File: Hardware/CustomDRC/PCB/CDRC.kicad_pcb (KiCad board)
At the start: 2 copper layers, 76.5 x 28.2 mm, 54 parts, among them IC301 SN65HVD75DR, J101 DSP Header, J401 TC2030NL - For UART PROG, J501 Conn_01x05, J504 Conn_01x05, Q501 AO3401A, Q502 AO3400A, U401 ESP32-WROOM-32UE-R2, U501 ESD224DQA, U502 ESD224DQA

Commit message: Update - finished schematic for revision A
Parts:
- removed JP301: SolderJumper_2_Open, Jumper:SolderJumper-2_P1.3mm_Open_RoundedPad1.0x1.5mm
- removed Q502: AO3400A, Package_TO_SOT_SMD:SOT-23
- added C201: 0u1, Capacitor_SMD:C_0603_1608Metric_Pad1.08x0.95mm_HandSolder, F.Cu at (153.0, 78.0)
- added C202: 10u, Capacitor_SMD:C_1206_3216Metric_Pad1.33x1.80mm_HandSolder, F.Cu at (154.0, 69.5)
- added C203: 10u, Capacitor_SMD:C_1206_3216Metric_Pad1.33x1.80mm_HandSolder, F.Cu at (154.0, 72.0)
- added C204: 22u, Capacitor_SMD:C_0805_2012Metric_Pad1.18x1.45mm_HandSolder, F.Cu at (147.5, 70.2)
- added C205: 22u, Capacitor_SMD:C_0805_2012Metric_Pad1.18x1.45mm_HandSolder, F.Cu at (147.5, 72.2)
- added C206: 2u2, Capacitor_SMD:C_0805_2012Metric_Pad1.18x1.45mm_HandSolder, F.Cu at (143.5, 75.0)
- added C207: 2u2, Capacitor_SMD:C_0805_2012Metric_Pad1.18x1.45mm_HandSolder, F.Cu at (137.5, 75.0)
- added C401: 1u, Capacitor_SMD:C_0603_1608Metric_Pad1.08x0.95mm_HandSolder, F.Cu at (118.0, 55.2)
- added C402: 22u, Capacitor_SMD:C_0805_2012Metric_Pad1.18x1.45mm_HandSolder, F.Cu at (113.5, 57.5)
- added C403: 1u, Capacitor_SMD:C_0603_1608Metric_Pad1.08x0.95mm_HandSolder, F.Cu at (115.5, 57.8)
- added D201: 1N4148WS, Diode_SMD:D_SOD-323_HandSoldering, F.Cu at (140.5, 72.0)
- added D202: US1M, Diode_SMD:D_SMA_Handsoldering, F.Cu at (158.2, 74.0)
- added D401: LED_Small, LED_SMD:LED_0603_1608Metric_Pad1.05x0.95mm_HandSolder, F.Cu at (126.0, 77.7)
- added F201: 2A TRIP, Fuse:Fuse_1206_3216Metric_Pad1.42x1.75mm_HandSolder, F.Cu at (161.5, 74.0)
- added F202: 1A TRIP, Fuse:Fuse_0603_1608Metric_Pad1.05x0.95mm_HandSolder, F.Cu at (137.5, 71.0)
- added H101: MountingHole, MountingHole:MountingHole_2.7mm_M2.5, F.Cu at (156.8, 55.2)
- added H102: MountingHole, MountingHole:MountingHole_2.7mm_M2.5, F.Cu at (97.8, 66.2)
- added H103: MountingHole, MountingHole:MountingHole_2.7mm_M2.5, F.Cu at (167.2, 76.8)
- added J502: JST-PH-2.0-02, Connector_JST:JST_PH_B2B-PH-K_1x02_P2.00mm_Vertical, F.Cu at (103.8, 67.2)
- added JP304: SolderJumper_3_Bridged12, Jumper:SolderJumper-3_P1.3mm_Bridged2Bar12_RoundedPad1.0x1.5mm, F.Cu at (144.8, 64.2)
- added L201: 4u7, Inductor_SMD:L_Chilisin_BMRA00040420, F.Cu at (148.5, 76.0)
- added R201: 0R, Resistor_SMD:R_0603_1608Metric_Pad0.98x0.95mm_HandSolder, F.Cu at (142.7, 68.6)
- added R401: 10k, Resistor_SMD:R_0603_1608Metric_Pad0.98x0.95mm_HandSolder, F.Cu at (114.5, 60.2)
- added R402: 330R, Resistor_SMD:R_0603_1608Metric_Pad0.98x0.95mm_HandSolder, F.Cu at (115.2, 76.2)
- added R403: 330R, Resistor_SMD:R_0603_1608Metric_Pad0.98x0.95mm_HandSolder, F.Cu at (138.5, 68.2)
- added TP101: TestPoint_Small, TestPoint:TestPoint_Keystone_5000-5004_Miniature, F.Cu at (163.5, 59.0)
- added TP102: TestPoint_Small, TestPoint:TestPoint_Pad_D1.5mm, F.Cu at (164.0, 71.8)
- added TP103: TestPoint_Small, TestPoint:TestPoint_Pad_D1.5mm, F.Cu at (155.8, 66.8)
- added TP201: TestPoint_Small, TestPoint:TestPoint_Pad_D1.5mm, F.Cu at (150.2, 68.2)
- added TP202: TestPoint_Small, TestPoint:TestPoint_Pad_D1.5mm, F.Cu at (135.0, 77.8)
- added TP203: TestPoint_Small, TestPoint:TestPoint_Pad_D1.5mm, F.Cu at (144.2, 71.2)
- added TP204: TestPoint_Small, TestPoint:TestPoint_Pad_D1.5mm, F.Cu at (158.2, 67.8)
- added TP401: TestPoint_Small, TestPoint:TestPoint_Pad_D1.5mm, F.Cu at (130.5, 78.0)
- added U201: AP63205WU-7, Package_TO_SOT_SMD:TSOT-23-6, F.Cu at (153.8, 75.0)
- added U202: TLV76733DRVR, Package_SON:WSON-6-1EP_2x2mm_P0.65mm_EP1x1.6mm_ThermalVias, F.Cu at (140.5, 74.5)
- C301: footprint Capacitor_SMD:C_0603_1608Metric -> Capacitor_SMD:C_0603_1608Metric_Pad1.08x0.95mm_HandSolder
- D301: value SM712_SOT23 -> SM712
- IC301: footprint Package_SO:SOIC-8_5.23x5.23mm_P1.27mm -> Package_SO:SOIC-8_3.9x4.9mm_P1.27mm
- J501, J504: value Conn_01x05 -> JST-PH-2.0-05
- Q501: value AO3401A -> AO3400A
- R501, R503: value 10k -> 330R
- R502, R504, R510, R511, R512, R515: value 330R -> 10k
- TP508: footprint TestPoint:TestPoint_Pad_D1.5mm -> TestPoint:TestPoint_Keystone_5000-5004_Miniature
- moved Q501 44.8 mm to (99.2, 71.0), turned to 90 degrees
- moved R505 40.1 mm to (96.5, 70.8), turned to -90 degrees
- moved R501 38.8 mm to (97.8, 61.2), turned to 0 degrees
- moved TP306 36.8 mm to (117.5, 77.8), turned to 0 degrees
- moved TP304 36.0 mm to (120.5, 77.8)
- moved R503 32.7 mm to (113.8, 76.2)
- moved TP301 27.1 mm to (140.2, 66.2)
- moved TP302 22.6 mm to (138.0, 65.0)
- moved TP307 18.6 mm to (158.0, 59.5)
- moved TP305 18.4 mm to (150.2, 56.8)
- moved TP303 16.5 mm to (140.2, 62.8)
- moved C301 8.73 mm to (154.8, 59.2), turned to 0 degrees
- moved R301 8.65 mm to (148.5, 58.8)
- moved IC301 8.57 mm to (151.5, 62.8)
- moved R302 8.57 mm to (158.0, 61.8)
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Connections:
- C301 pad 1: Net-(IC301-VCC) -> VCC
- C501 pad 1: /USER_INTERFACE/ENCODER_1_B -> /MCU/IO32
- C502 pad 1: /USER_INTERFACE/ENCODER_1_A -> /MCU/IO35
- C503 pad 1: /USER_INTERFACE/ENCODER_2_B -> /MCU/GPIO39
- C504 pad 1: /USER_INTERFACE/ENCODER_2_A -> /MCU/GPIO36
- C505 pad 1: /USER_INTERFACE/ENCODER_1_SW -> /MCU/IO33
- C506 pad 1: /USER_INTERFACE/ENCODER_2_SW -> /MCU/IO34
- IC301 pad 1: /RS485/RX485_RX -> /MCU/IO21
- IC301 pad 2: /RS485/RS485_TX_EN -> /RS485/~{RE}
- IC301 pad 3: /RS485/RS485_TX_EN -> /MCU/IO19
- IC301 pad 4: /RS485/RX485_TX -> /MCU/IO18
- IC301 pad 8: Net-(IC301-VCC) -> VCC
- J101 pad 1: GND -> unconnected-(J101-Pin_1-Pad1)
- J101 pad 3: /DSP_RS485_B/Z -> GND
- J101 pad 4: /DSP_RS485_A/Y -> /DSP_RS485_B/Z
- J101 pad 5: /DSP_POWER_EN -> /DSP_RS485_A/Y
- J101 pad 6: /DSP_CONST_12V -> /DSP_POWER_EN
- J101 pad 7: unconnected-(J101-Pin_7-Pad7) -> /DSP_CONST_12V
- J501 pad 1: /USER_INTERFACE/ENC_3_A -> /USER_INTERFACE/ENC_2_A
- Q501 pad 2: VCC -> GND
- Q501 pad 3: VCC_ENCODER -> Net-(J502-Pin_1)
- R301 pad 1: Net-(IC301-VCC) -> VCC
- R301 pad 2: /RS485/RX485_RX -> /MCU/IO21
- R305 pad 1: /RS485/RS485_TX_EN -> /MCU/IO19
- R501 pad 1: VCC -> +5V
- R501 pad 2: Net-(Q501-G) -> Net-(J502-Pin_2)
- R502 pad 1: /USER_INTERFACE/ENC_1_B -> /MCU/IO32
- R502 pad 2: /USER_INTERFACE/ENCODER_1_B -> /USER_INTERFACE/ENC_1_B
- R503 pad 1: /USER_INTERFACE/ENCODER_PWR_EN -> /MCU/IO25
- R503 pad 2: GND -> Net-(Q501-G)
- R504 pad 2: /USER_INTERFACE/ENCODER_1_A -> /MCU/IO35
- R505 pad 1: Net-(Q502-G) -> GND
- R505 pad 2: /USER_INTERFACE/ENCODER_PWR_EN -> Net-(Q501-G)
- R506 pad 1: /USER_INTERFACE/ENCODER_1_A -> /USER_INTERFACE/ENC_1_A
- R506 pad 2: VCC_ENCODER -> VCC
- R507 pad 1: /USER_INTERFACE/ENCODER_1_B -> /USER_INTERFACE/ENC_1_B
- R507 pad 2: VCC_ENCODER -> VCC
- R508 pad 1: /USER_INTERFACE/ENCODER_2_B -> /USER_INTERFACE/ENC_2_B
- R508 pad 2: VCC_ENCODER -> VCC
- R509 pad 1: /USER_INTERFACE/ENCODER_2_A -> /USER_INTERFACE/ENC_2_A
- R509 pad 2: VCC_ENCODER -> VCC
- R510 pad 1: /USER_INTERFACE/ENC_2_B -> /MCU/GPIO39
- R510 pad 2: /USER_INTERFACE/ENCODER_2_B -> /USER_INTERFACE/ENC_2_B
- R511 pad 1: /USER_INTERFACE/ENC_3_A -> /USER_INTERFACE/ENC_2_A
- R511 pad 2: /USER_INTERFACE/ENCODER_2_A -> /MCU/GPIO36
- R512 pad 1: /USER_INTERFACE/ENC_1_SW -> /MCU/IO33
- R512 pad 2: /USER_INTERFACE/ENCODER_1_SW -> /USER_INTERFACE/ENC_1_SW
- R513 pad 1: /USER_INTERFACE/ENCODER_1_SW -> /USER_INTERFACE/ENC_1_SW
- R514 pad 1: /USER_INTERFACE/ENCODER_2_SW -> /USER_INTERFACE/ENC_2_SW
- R515 pad 1: /USER_INTERFACE/ENC_2_SW -> /MCU/IO34
- R515 pad 2: /USER_INTERFACE/ENCODER_2_SW -> /USER_INTERFACE/ENC_2_SW
- TP301 pad 1: /RS485/RX485_TX -> /MCU/IO18
- TP302 pad 1: /RS485/RS485_TX_EN -> /MCU/IO19
- TP303 pad 1: /RS485/RX485_RX -> /MCU/IO21
- TP304 pad 1: /DSP_RS485_B/Z -> Net-(U401-IO26)
- TP305 pad 1: Net-(IC301-VCC) -> VCC
- TP306 pad 1: /DSP_RS485_A/Y -> Net-(U401-IO27)
- TP501 pad 1: /USER_INTERFACE/ENCODER_1_B -> /MCU/IO32
- TP502 pad 1: /USER_INTERFACE/ENCODER_1_A -> /MCU/IO35
- TP503 pad 1: /USER_INTERFACE/ENCODER_1_SW -> /MCU/IO33
- TP504 pad 1: /USER_INTERFACE/ENCODER_2_B -> /MCU/GPIO39
- TP505 pad 1: /USER_INTERFACE/ENCODER_2_A -> /MCU/GPIO36
- TP506 pad 1: /USER_INTERFACE/ENCODER_2_SW -> /MCU/IO34
- U401 pad 10: unconnected-(U401-IO25-Pad10) -> /MCU/IO25
- U401 pad 11: unconnected-(U401-IO26-Pad11) -> Net-(U401-IO26)
- U401 pad 12: unconnected-(U401-IO27-Pad12) -> Net-(U401-IO27)
- U401 pad 16: unconnected-(U401-IO13-Pad16) -> Net-(U401-IO13)
- U401 pad 29: unconnected-(U401-IO5-Pad29) -> /MCU/DSP_EN
- U401 pad 30: unconnected-(U401-IO18-Pad30) -> /MCU/IO18
- U401 pad 31: unconnected-(U401-IO19-Pad31) -> /MCU/IO19
- U401 pad 33: unconnected-(U401-IO21-Pad33) -> /MCU/IO21
- U401 pad 4: unconnected-(U401-SENSOR_VP-Pad4) -> /MCU/GPIO36
- U401 pad 5: unconnected-(U401-SENSOR_VN-Pad5) -> /MCU/GPIO39
- U401 pad 6: unconnected-(U401-IO34-Pad6) -> /MCU/IO34
- U401 pad 7: unconnected-(U401-IO35-Pad7) -> /MCU/IO35
- U401 pad 8: unconnected-(U401-IO32-Pad8) -> /MCU/IO32
- U401 pad 9: unconnected-(U401-IO33-Pad9) -> /MCU/IO33
- U502 pad 1: /USER_INTERFACE/ENC_3_A -> /USER_INTERFACE/ENC_2_A
- U502 pad 10: /USER_INTERFACE/ENC_3_A -> /USER_INTERFACE/ENC_2_A
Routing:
- net VCC: track 0.00 -> 136.6 mm
- net +5V: track 0.00 -> 100.8 mm
- net GND: track 0.00 -> 49.1 mm, vias 0 -> 45
- net /MCU/ESP_EN: track 0.00 -> 44.3 mm
- net /MCU/ESP_BOOT0: track 0.00 -> 29.4 mm
- net /DSP_POWER_EN: track 0.00 -> 29.2 mm
- net Net-(Q501-G): track 0.00 -> 28.6 mm
- net /USER_INTERFACE/ENC_2_B: track 0.00 -> 21.1 mm
- net /USER_INTERFACE/ENC_2_SW: track 0.00 -> 20.5 mm
- net /USER_INTERFACE/ENC_1_A: track 0.00 -> 19.6 mm
- net /MCU/IO19: track 0.00 -> 19.2 mm
- net /MCU/IO21: track 0.00 -> 18.8 mm
- net /USER_INTERFACE/ENC_1_SW: track 0.00 -> 18.3 mm
- net /USER_INTERFACE/ENC_2_A: track 0.00 -> 17.3 mm
- net /MCU/IO18: track 0.00 -> 16.5 mm
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- added copper zone on F.Cu, net +5V
- added copper zone on F.Cu, net /DSP_CONST_12V
- added copper zone on B.Cu, net GND
- added copper zone on F.Cu, net GND
- added copper zone on F.Cu, net Net-(D201-A)
- added copper zone on F.Cu, net Net-(D202-A)
- added copper zone on F.Cu, net Net-(D202-K)
- added copper zone on F.Cu, net Net-(F202-Pad2)
- added copper zone on F.Cu, net Net-(U201-SW)
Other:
- board size 76.5 x 28.2 mm -> 85 x 28.5 mm
- board text added: "${TITLE}-${REVISION} ${ISSUE_DATE}"
- board text added: "+"
- board text added: "-"
- board text added: "12V BLUE"
- board text added: "1A"
- board text added: "1B"
- board text added: "1SW"
- board text added: "2A"
- board text added: "2B"
- board text added: "2SW"
- board text added: "A/Y GREEN"
- board text added: "B/Z RED"
- board text added: "BLACK"
- board text added: "BLUE"
- board text added: "DNC"
- board text added: "ENC1"
- board text added: "ENC2"
- board text added: "GND"
- board text added: "GND BLACK"
- board text added: "GND WHITE"
- board text added: "GND YELLOW"
- board text added: "GREEN"
- board text added: "JAIME SEQUEIRA"
- board text added: "JLCJLCJLCJLC"
- board text added: "LED"
- board text added: "LED+"
- board text added: "LED-"
- board text added: "PROG"
- board text added: "RED"
- board text added: "WHITE"
- board text added: "YELLOW"

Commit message: Sync HW changes for V1 PCB
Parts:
- removed C206, C207: 2u2, Capacitor_SMD:C_0805_2012Metric_Pad1.18x1.45mm_HandSolder
- removed D201: 1N4148WS, Diode_SMD:D_SOD-323_HandSoldering
- removed F202: 1A TRIP, Fuse:Fuse_0603_1608Metric_Pad1.05x0.95mm_HandSolder
- removed TP202, TP305, TP307: TestPoint_Small, TestPoint:TestPoint_Pad_D1.5mm
- removed U202: TLV76733DRVR, Package_SON:WSON-6-1EP_2x2mm_P0.65mm_EP1x1.6mm_ThermalVias
- added R516: 330R, Resistor_SMD:R_1206_3216Metric_Pad1.30x1.75mm_HandSolder, F.Cu at (127.2, 87.5)
- D401: value LED_Small -> WHITE OR BLUE
- F201: value 2A TRIP -> BSMD1206-025-33V
- L201: footprint Inductor_SMD:L_Chilisin_BMRA00040420 -> Inductor_SMD:L_Cenker_CKCS4030
- U201: value AP63205WU-7 -> AP63203WU-7
- moved R201 40.9 mm to (173.8, 95.2)
- moved R403 40.0 mm to (168.0, 95.2)
- moved C503 39.5 mm to (141.5, 88.5)
- moved C501 39.5 mm to (141.5, 99.1)
- moved C502 39.5 mm to (141.5, 95.6)
- moved C505 39.5 mm to (141.5, 102.7)
- moved C506 39.5 mm to (141.5, 92.0)
- moved J101 39.5 mm to (196.8, 82.8)
- moved C201 39.5 mm to (182.5, 104.2)
- moved C202 39.5 mm to (183.5, 95.8)
- moved C203 39.5 mm to (183.5, 98.2)
- moved C204 39.5 mm to (177.0, 96.5)
- moved C205 39.5 mm to (177.0, 98.5)
- moved C301 39.5 mm to (184.2, 85.5)
- moved C401 39.5 mm to (147.5, 81.5)
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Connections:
- C204 pad 1: +5V -> VCC
- C205 pad 1: +5V -> VCC
- L201 pad 2: +5V -> VCC
- R201 pad 1: Net-(F202-Pad2) -> VCC
- R501 pad 1: +5V -> VCC
- TP203 pad 1: +5V -> VCC
- U201 pad 1: +5V -> VCC
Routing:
- net +5V: track 100.8 -> 0.00 mm
- net VCC: track 136.6 -> 168.5 mm
- net /MCU/IO19: track 19.2 -> 16.8 mm
- net /RS485/RS485_B: track 5.29 -> 3.26 mm
- net /RS485/RS485_A: track 4.79 -> 3.26 mm
- net /DSP_RS485_A/Y: track 14.6 -> 13.1 mm
- net GND: track 49.1 -> 47.7 mm, vias 45 -> 34
- net /MCU/ESP_EN: track 44.3 -> 43.1 mm
- net Net-(U201-SW): track 3.70 -> 2.56 mm
- net /MCU/IO34: track 9.21 -> 8.63 mm
- added copper zone on F.Cu, net VCC
- removed copper zone on F.Cu, net +5V
- removed copper zone on F.Cu, net Net-(D201-A)
- removed copper zone on F.Cu, net Net-(F202-Pad2)
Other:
- board text added: "MNT"

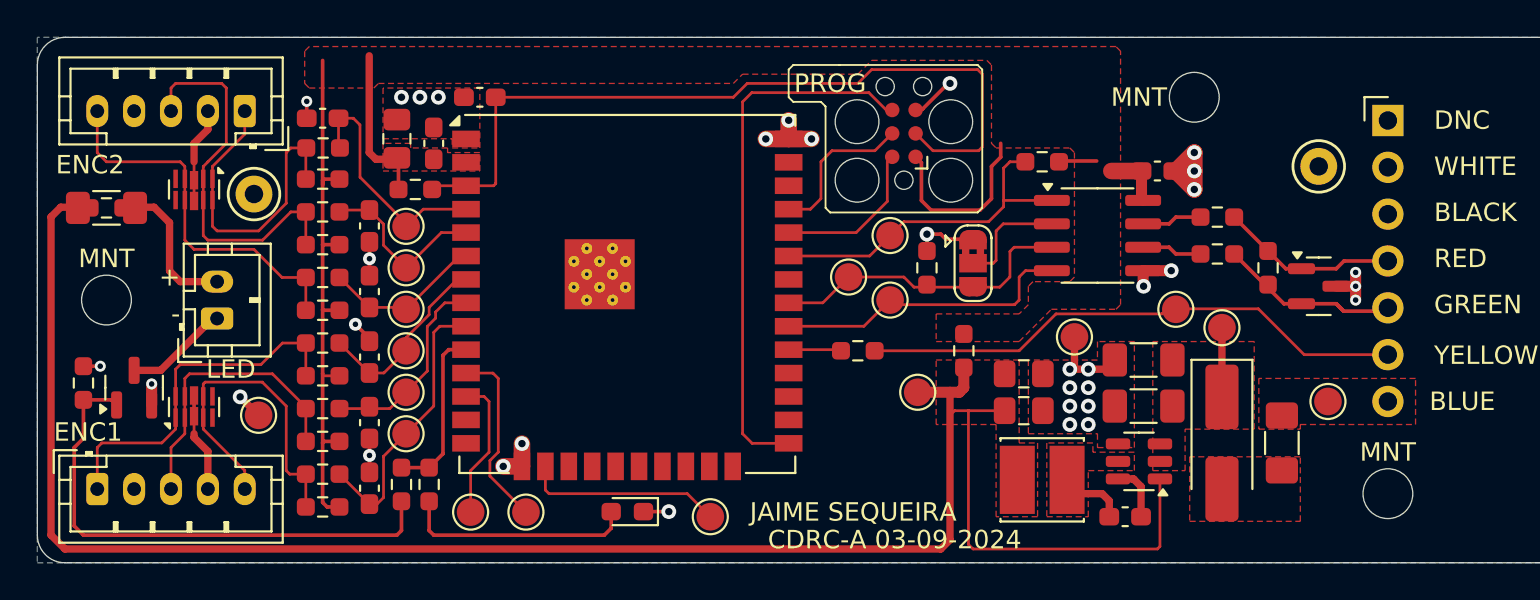
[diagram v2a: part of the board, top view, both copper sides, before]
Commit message: Sync before making breaking changes to RS485 comms protocl and method
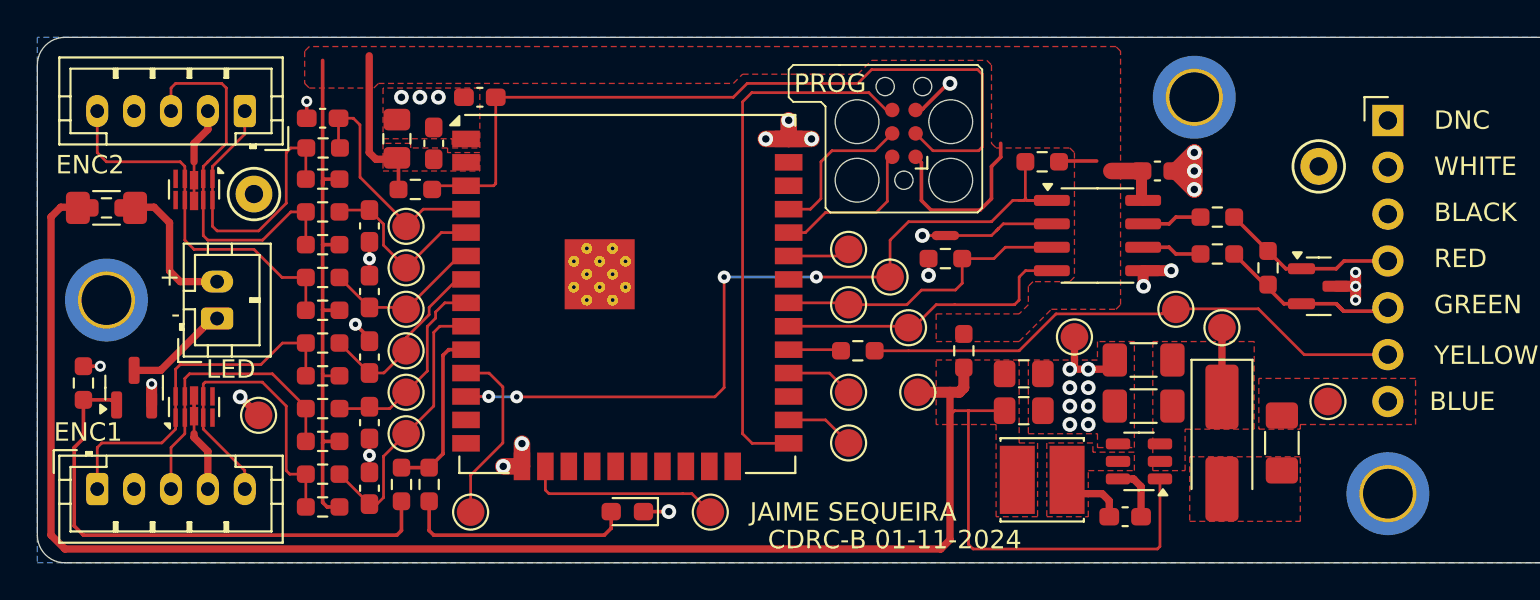
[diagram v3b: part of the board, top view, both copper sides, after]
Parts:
- removed JP304: SolderJumper_3_Bridged12, Jumper:SolderJumper-3_P1.3mm_Bridged2Bar12_RoundedPad1.0x1.5mm
- removed TP401: TestPoint_Small, TestPoint:TestPoint_Pad_D1.5mm
- added NT1: NetTie_2, NetTie:NetTie-2_SMD_Pad0.5mm, F.Cu at (172.8, 89.0)
- added TP305: TestPoint_Small, TestPoint:TestPoint_Pad_D1.5mm, F.Cu at (167.5, 97.5)
- added TP307: TestPoint_Small, TestPoint:TestPoint_Pad_D1.5mm, F.Cu at (167.5, 100.2)
- added TP308: TestPoint_Small, TestPoint:TestPoint_Pad_D1.5mm, F.Cu at (160.0, 104.0)
- H101, H102, H103: footprint MountingHole:MountingHole_2.7mm_M2.5 -> MountingHole:MountingHole_2.7mm_M2.5_ISO7380_Pad_TopOnly; moved to B.Cu
- L201: value 4u7 -> 3u9
- moved TP306 25.0 mm to (167.5, 89.8)
- moved TP304 3.00 mm to (147.0, 104.0)
- moved TP303 2.25 mm to (169.8, 91.2)
- moved TP301 1.80 mm to (170.8, 94.0)
- moved TP302 1.50 mm to (167.5, 92.8)
- moved R305 1.12 mm to (172.8, 90.2), turned to 180 degrees
- turned H101 to 180 degrees
- turned H102 to 180 degrees
- turned H103 to 180 degrees
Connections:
- net /MCU/GPIO36 renamed /MCU/IO36
- net /MCU/GPIO39 renamed /MCU/IO39
- IC301 pad 1: /MCU/IO21 -> /MCU/IO27
- R301 pad 2: /MCU/IO21 -> /MCU/IO27
- TP303 pad 1: /MCU/IO21 -> /MCU/IO27
- TP306 pad 1: Net-(U401-IO27) -> Net-(U401-IO21)
- U401 pad 12: Net-(U401-IO27) -> /MCU/IO27
- U401 pad 26: unconnected-(U401-IO4-Pad26) -> Net-(U401-IO4)
- U401 pad 28: unconnected-(U401-IO17-Pad28) -> Net-(U401-IO17)
- U401 pad 33: /MCU/IO21 -> Net-(U401-IO21)
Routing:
- net /MCU/IO27: track 0.00 -> 44.7 mm, vias 0 -> 4
- net /MCU/IO21: track 18.8 -> 0.00 mm
- net Net-(U401-IO27): track 7.78 -> 0.00 mm
- net Net-(U401-IO4): track 0.00 -> 3.77 mm
- net Net-(U401-IO17): track 0.00 -> 3.68 mm
- net Net-(U401-IO21): track 0.00 -> 3.40 mm
- net GND: track 47.7 -> 45.8 mm, vias 34 -> 35
- net /DSP_RS485_A/Y: track 13.1 -> 12.4 mm

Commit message: Sync changes to Rev B HW
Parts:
- removed TP201, TP507: TestPoint_Small, TestPoint:TestPoint_Pad_D1.5mm
- added H104: MountingHole, MountingHole:MountingHole_2.7mm_M2.5_ISO7380_Pad_TopBottom, B.Cu at (190.0, 114.8)
- H101, H102, H103: footprint MountingHole:MountingHole_2.7mm_M2.5_ISO7380_Pad_TopOnly -> MountingHole:MountingHole_2.7mm_M2.5_ISO7380_Pad_TopBottom
- J101: footprint Connector_PinHeader_2.54mm:PinHeader_1x07_P2.54mm_Horizontal -> CDRC_Footprints:M208900705
- J501, J504: value JST-PH-2.0-05 -> JST_PH_S5B-PH-SM4; footprint Connector_JST:JST_PH_B5B-PH-K_1x05_P2.00mm_Vertical -> Connector_JST:JST_PH_S5B-PH-SM4-TB_1x05-1MP_P2.00mm_Horizontal
- J502: value JST-PH-2.0-02 -> ST_PH_S2B-PH-SM4; footprint Connector_JST:JST_PH_B2B-PH-K_1x02_P2.00mm_Vertical -> Connector_JST:JST_PH_S2B-PH-SM4-TB_1x02-1MP_P2.00mm_Horizontal
- moved H103 77.2 mm to (122.5, 81.8)
- moved H101 71.9 mm to (122.5, 114.8)
- moved H102 63.7 mm to (190.0, 81.8)
- moved R301 44.7 mm to (137.8, 104.5), turned to 90 degrees
- moved J501 34.9 mm to (114.0, 110.2), turned to -90 degrees
- moved TP204 27.3 mm to (172.0, 116.2)
- moved D401 26.4 mm to (131.0, 94.2), turned to 0 degrees
- moved J504 20.9 mm to (114.0, 86.2), turned to -90 degrees
- moved TP101 20.0 mm to (176.0, 95.8)
- moved J502 19.8 mm to (114.0, 98.2), turned to -90 degrees
- moved R302 19.8 mm to (170.8, 98.5)
- moved R304 19.8 mm to (170.8, 100.5)
- moved IC301 19.1 mm to (165.0, 99.5)
- moved R303 19.1 mm to (173.2, 99.5)
- moved C301 18.8 mm to (168.5, 95.8)
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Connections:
- J101 pad 1: unconnected-(J101-Pin_1-Pad1) -> /DSP_CONST_12V
- J101 pad 2: GND -> /DSP_POWER_EN
- J101 pad 3: GND -> /DSP_RS485_A/Y
- J101 pad 5: /DSP_RS485_A/Y -> GND
- J101 pad 6: /DSP_POWER_EN -> GND
- J101 pad 7: /DSP_CONST_12V -> unconnected-(J101-Pin_7-Pad7)
- J501 pad 1: /USER_INTERFACE/ENC_2_A -> /USER_INTERFACE/ENC_1_A
- J501 pad 3: /USER_INTERFACE/ENC_2_B -> /USER_INTERFACE/ENC_1_B
- J501 pad 5: /USER_INTERFACE/ENC_2_SW -> /USER_INTERFACE/ENC_1_SW
- J504 pad 1: /USER_INTERFACE/ENC_1_A -> /USER_INTERFACE/ENC_2_A
- J504 pad 3: /USER_INTERFACE/ENC_1_B -> /USER_INTERFACE/ENC_2_B
- J504 pad 5: /USER_INTERFACE/ENC_1_SW -> /USER_INTERFACE/ENC_2_SW
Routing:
- net VCC: track 168.5 -> 237.1 mm
- net Net-(Q501-G): track 28.6 -> 4.10 mm
- net GND: track 45.8 -> 27.1 mm, vias 35 -> 192
- net /DSP_POWER_EN: track 29.3 -> 17.1 mm
- net /MCU/IO19: track 16.4 -> 6.62 mm
- net /MCU/IO32: track 10.9 -> 19.9 mm
- net Net-(D401-A): track 12.6 -> 3.92 mm
- net /MCU/IO33: track 14.8 -> 23.4 mm
- net Net-(U401-IO17): track 3.68 -> 11.7 mm
- net Net-(U401-IO13): track 10.7 -> 2.89 mm
- net /MCU/IO18: track 16.5 -> 8.75 mm
- net /MCU/DSP_EN: track 2.86 -> 10.5 mm
- net /MCU/IO25: track 9.28 -> 16.4 mm, vias 0 -> 2
- net Net-(U401-IO26): track 9.83 -> 3.56 mm
- net /MCU/IO39: track 9.52 -> 15.4 mm
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- added copper zone on F.Cu, net /USER_INTERFACE/MNT
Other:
- board size 85 x 28.5 mm -> 85 x 40 mm
- board text added: "ANT"
- board text added: "ENC_1A"
- board text added: "ENC_1B"
- board text added: "ENC_1SW"
- board text added: "ENC_2A"
- board text added: "ENC_2B"
- board text added: "ENC_2SW"
- board text added: "NC"
- board text removed: "+"
- board text removed: "-"
- board text removed: "12V BLUE"
- board text removed: "1A"
- board text removed: "1B"
- board text removed: "1SW"
- board text removed: "2A"
- board text removed: "2B"
- board text removed: "2SW"
- board text removed: "A/Y GREEN"
- board text removed: "B/Z RED"
- board text removed: "DNC"
- board text removed: "ENC1"
- board text removed: "ENC2"
- board text removed: "GND BLACK"
- board text removed: "GND WHITE"
- board text removed: "GND YELLOW"
- board text removed: "LED"
- board text removed: "MNT"
- board text removed: "PROG"
